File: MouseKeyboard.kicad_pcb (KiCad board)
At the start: 2 copper layers, 83.8 x 55.9 mm, 20 parts, among them IC1 ATMEGA328P-P, J1 USB, SW1 SW_PUSH, SW2 SW_PUSH, SW3 SW_PUSH, SW4 SW_PUSH, SW5 SW_PUSH, SW6 SW_PUSH, SW7 SW_PUSH, SW8 SPST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

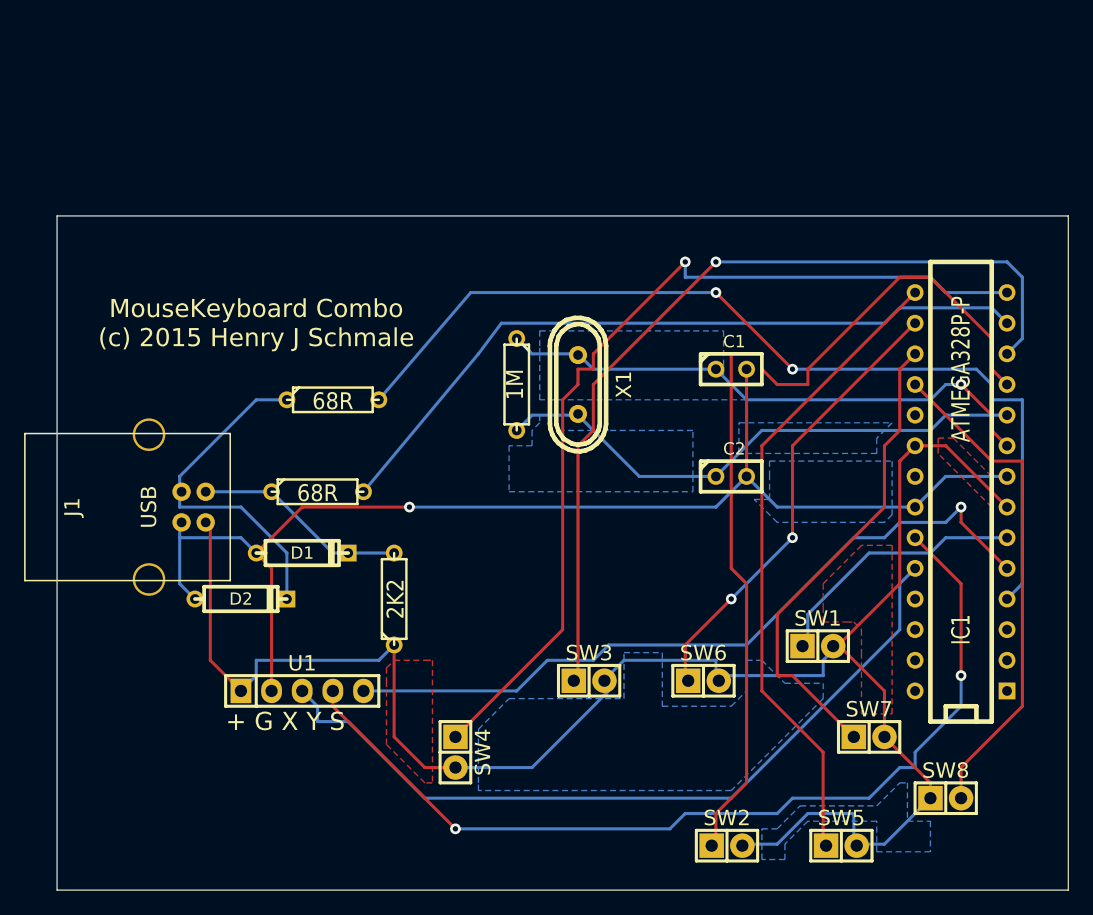
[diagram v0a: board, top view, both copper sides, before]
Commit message: Shrunk the PCB Design
* The PCB is roughly 20% Smaller than before
* \todo fix autorouting errors
* \todo perform DRC
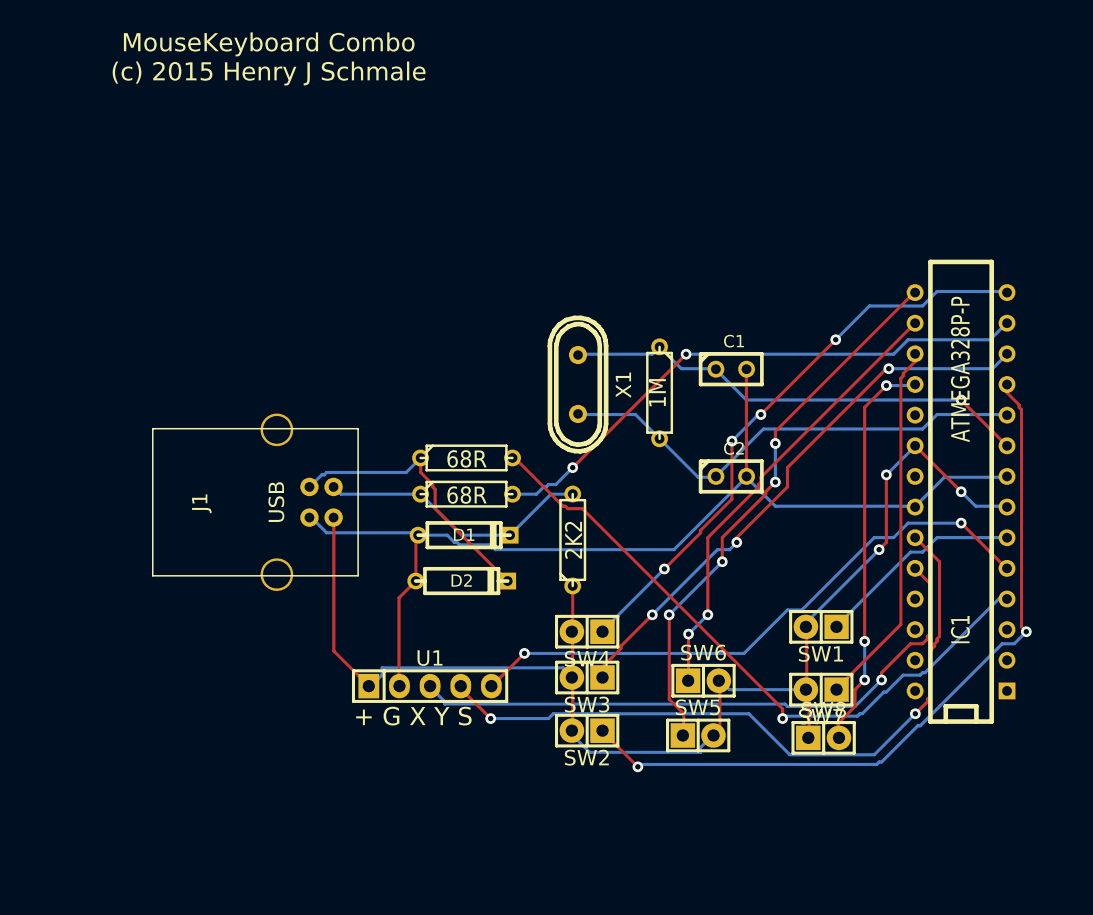
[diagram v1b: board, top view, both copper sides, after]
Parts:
- moved D2 18.4 mm to (132.6, 109.0)
- moved R1 15.6 mm to (141.8, 105.6)
- moved SW2 15.0 mm to (143.0, 121.4), turned to 180 degrees
- moved SW5 15.0 mm to (152.2, 121.8)
- moved SW4 14.8 mm to (143.0, 113.2), turned to 180 degrees
- moved D1 13.5 mm to (132.8, 105.2)
- moved R3 12.4 mm to (133.0, 101.8)
- moved R2 12.1 mm to (133.0, 98.8)
- moved R4 11.9 mm to (149.0, 93.4)
- moved SW8 11.3 mm to (162.6, 122.0)
- moved J1 10.6 mm to (117.3, 102.5)
- moved U1 10.6 mm to (130.0, 117.7)
- moved SW7 5.58 mm to (162.4, 118.0), turned to 180 degrees
- moved SW1 1.62 mm to (162.4, 112.8), turned to 180 degrees
- moved SW3 0.31 mm to (143.0, 117.0), turned to 180 degrees
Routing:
- net +5V: track 152.9 -> 110.4 mm, vias 0 -> 3
- net Net-(IC1-Pad14): track 76.5 -> 48.4 mm, vias 1 -> 4
- net Net-(IC1-Pad12): track 72.4 -> 46.6 mm, vias 1 -> 3
- net Net-(IC1-Pad4): track 78.9 -> 54.6 mm, vias 2 -> 1
- net Net-(IC1-Pad23): track 78.0 -> 58.2 mm
- net GND: track 101.9 -> 86.3 mm, vias 1 -> 0
- net Net-(IC1-Pad11): track 76.8 -> 62.3 mm, vias 0 -> 2
- net Net-(IC1-Pad24): track 65.3 -> 51.2 mm, vias 0 -> 1
- net Net-(IC1-Pad13): track 61.0 -> 46.9 mm, vias 0 -> 2
- net Net-(IC1-Pad5): track 62.5 -> 50.2 mm, vias 1 -> 2
- net Net-(IC1-Pad17): track 39.9 -> 30.6 mm
- net Net-(IC1-Pad18): track 41.6 -> 33.4 mm, vias 0 -> 3
- net Net-(IC1-Pad15): track 53.4 -> 45.9 mm, vias 0 -> 4
- net XTAL1: track 46.3 -> 39.5 mm
- net XTAL2: track 45.6 -> 40.0 mm
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- removed copper zone on B.Cu, net +5V
- removed copper zone on F.Cu, net +5V
- removed copper zone on B.Cu, net GND
- removed copper zone on B.Cu, net XTAL1
- removed copper zone on B.Cu, net XTAL2
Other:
- board outline removed

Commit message: Improved PCB Design
* Changed Text Size
* Moved Text Around
* DRC
* Improoved Routing

\todo Copper Infill
\todo Dimensioning
\todo Board Cut Lines
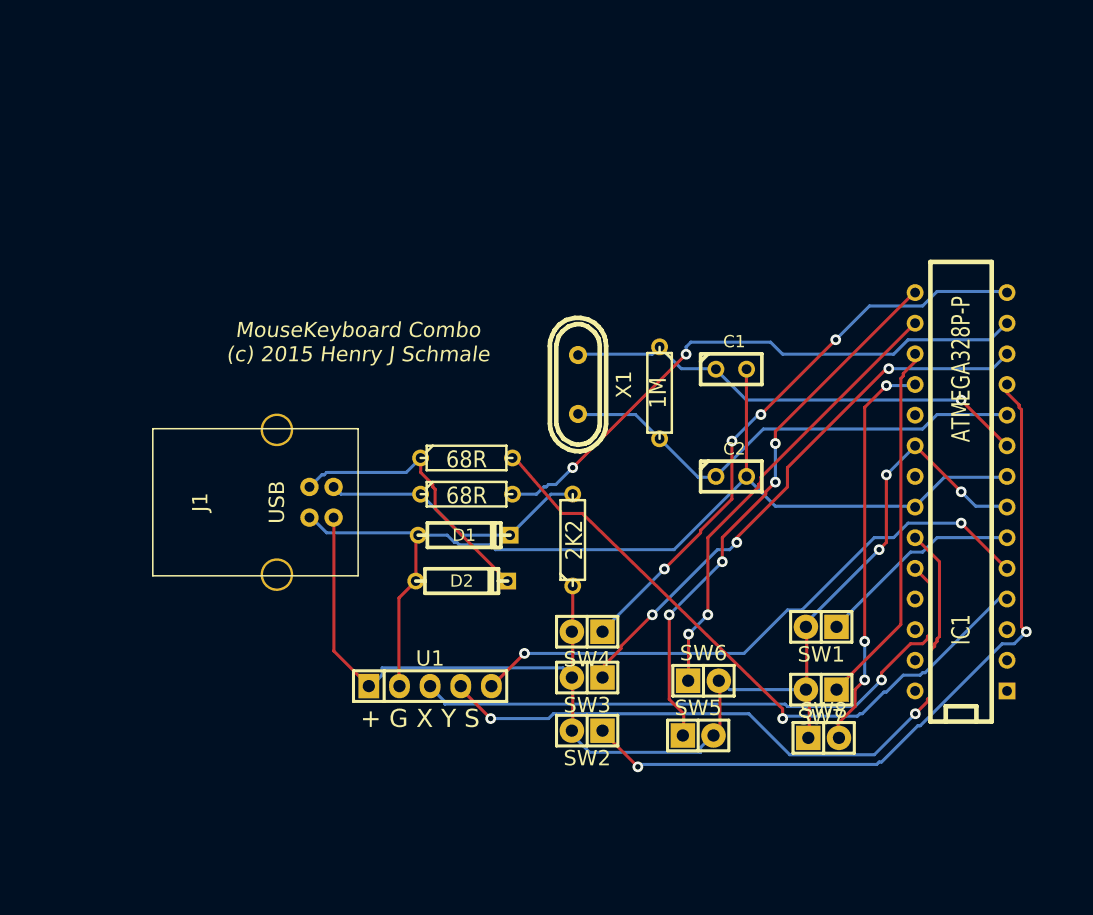
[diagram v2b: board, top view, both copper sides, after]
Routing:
- net Net-(IC1-Pad13): track 46.9 -> 48.1 mm
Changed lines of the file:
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@@
     (links 43)
     (no_connects 0)
-    (area 101.2 62.8 181.2 125)
+    (area 106.6 82 181 125.2)
     (thickness 1.6)
     (drawings 2)
-    (tracks 340)
+    (tracks 344)
     (zones 0)
     (modules 20)
@@
       (net 3 XTAL2))
   )
-  (gr_text "+ G X Y S\n" (at 123.63 120.25) (layer F.SilkS)
+  (gr_text "+ G X Y S\n" (at 124.2 120.4) (layer F.SilkS)
     (effects (font (size 1.5 1.5) (thickness 0.3)) (justify left))
   )
-  (gr_text "MouseKeyboard Combo\n(c) 2015 Henry J Schmale" (at 116.6 65.6) (layer F.SilkS)
-    (effects (font (size 1.5 1.5) (thickness 0.3)))
+  (gr_text "MouseKeyboard Combo\n(c) 2015 Henry J Schmale" (at 124 89.2) (layer F.SilkS)
+    (effects (font (size 1.25 1.25) (thickness 0.25) italic))
   )
   (segment (start 153.67 91.44) (end 153.6 91.4) (width 0.254) (layer B.Cu) (net 1) (status 80000))
@@
   (segment (start 120 101.2) (end 119.98002 101.2) (width 0.254) (layer B.Cu) (net 5) (status 80000))
   (segment (start 136.81 98.8) (end 137 98.8) (width 0.254) (layer F.Cu) (net 8) (status 80000))
-  (segment (start 137 98.8) (end 141 102.8) (width 0.254) (layer F.Cu) (net 8) (status 80000))
-  (segment (start 141 102.8) (end 141.2 102.8) (width 0.254) (layer F.Cu) (net 8) (status 80000))
-  (segment (start 141.2 102.8) (end 141.4 103) (width 0.254) (layer F.Cu) (net 8) (status 80000))
-  (segment (start 141.4 103) (end 142.6 103) (width 0.254) (layer F.Cu) (net 8) (status 80000))
-  (segment (start 142.6 103) (end 159.2 119.6) (width 0.254) (layer F.Cu) (net 8) (status 80000))
+  (segment (start 137 98.8) (end 140.8 103.2) (width 0.254) (layer F.Cu) (net 8) (status 80000))
+  (segment (start 140.8 103.2) (end 140.8 103.4) (width 0.254) (layer F.Cu) (net 8) (status 80000))
+  (segment (start 140.8 103.4) (end 141.2 103.4) (width 0.254) (layer F.Cu) (net 8) (status 80000))
+  (segment (start 141.2 103.4) (end 142.6 103.4) (width 0.254) (layer F.Cu) (net 8) (status 80000))
+  (segment (start 142.6 103.4) (end 159.2 119.6) (width 0.254) (layer F.Cu) (net 8) (status 80000))
   (segment (start 159.2 119.6) (end 159.2 120.4) (width 0.254) (layer F.Cu) (net 8) (status 80000))
   (via (at 159.2 120.4) (size 0.889) (layers F.Cu B.Cu) (net 8) (status 80000))
@@
   (segment (start 144.2 116.2) (end 144.2 117) (width 0.254) (layer F.Cu) (net 13) (status 80000))
   (segment (start 144.2 117) (end 144.27 117) (width 0.254) (layer F.Cu) (net 13) (status 80000))
+  (segment (start 151.2 90.2) (end 151.2 89.6) (width 0.254) (layer B.Cu) (net 14))
+  (segment (start 136.81 101.8) (end 138.8 101.8) (width 0.254) (layer B.Cu) (net 14) (status 80000))
+  (segment (start 139.4 101.2) (end 138.8 101.8) (width 0.254) (layer B.Cu) (net 14) (status 80000))
+  (segment (start 139.6 101.2) (end 139.4 101.2) (width 0.254) (layer B.Cu) (net 14) (status 80000))
+  (segment (start 139.8 101) (end 139.6 101.2) (width 0.254) (layer B.Cu) (net 14) (status 80000))
+  (segment (start 140.4 101) (end 139.8 101) (width 0.254) (layer B.Cu) (net 14) (status 80000))
+  (segment (start 141.8 99.6) (end 140.4 101) (width 0.254) (layer B.Cu) (net 14) (status 80000))
+  (via (at 141.8 99.6) (size 0.889) (layers F.Cu B.Cu) (net 14) (status 80000))
+  (segment (start 151.2 90.2) (end 141.8 99.6) (width 0.254) (layer F.Cu) (net 14) (status 80000))
+  (via (at 151.2 90.2) (size 0.889) (layers F.Cu B.Cu) (net 14) (status 80000))
+  (segment (start 168.4 90.2) (end 159.2 90.2) (width 0.254) (layer B.Cu) (net 14) (status 80000))
+  (segment (start 169.6 89) (end 168.4 90.2) (width 0.254) (layer B.Cu) (net 14) (status 80000))
+  (segment (start 176.4 89) (end 169.6 89) (width 0.254) (layer B.Cu) (net 14) (status 80000))
+  (segment (start 176.4 89) (end 177.8 87.6) (width 0.254) (layer B.Cu) (net 14) (status 80000))
+  (segment (start 158.2 89.2) (end 159.2 90.2) (width 0.254) (layer B.Cu) (net 14))
+  (segment (start 151.6 89.2) (end 158.2 89.2) (width 0.254) (layer B.Cu) (net 14))
+  (segment (start 151.2 89.6) (end 151.6 89.2) (width 0.254) (layer B.Cu) (net 14))
   (segment (start 177.8 87.63) (end 177.8 87.6) (width 0.254) (layer B.Cu) (net 14) (status 80000))
-  (segment (start 177.8 87.6) (end 176.4 89) (width 0.254) (layer B.Cu) (net 14) (status 80000))
-  (segment (start 176.4 89) (end 169.6 89) (width 0.254) (layer B.Cu) (net 14) (status 80000))
-  (segment (start 169.6 89) (end 168.4 90.2) (width 0.254) (layer B.Cu) (net 14) (status 80000))
-  (segment (start 168.4 90.2) (end 151.2 90.2) (width 0.254) (layer B.Cu) (net 14) (status 80000))
-  (via (at 151.2 90.2) (size 0.889) (layers F.Cu B.Cu) (net 14) (status 80000))
-  (segment (start 151.2 90.2) (end 141.8 99.6) (width 0.254) (layer F.Cu) (net 14) (status 80000))
-  (via (at 141.8 99.6) (size 0.889) (layers F.Cu B.Cu) (net 14) (status 80000))
-  (segment (start 141.8 99.6) (end 140.4 101) (width 0.254) (layer B.Cu) (net 14) (status 80000))
-  (segment (start 140.4 101) (end 139.8 101) (width 0.254) (layer B.Cu) (net 14) (status 80000))
-  (segment (start 139.8 101) (end 139.6 101.2) (width 0.254) (layer B.Cu) (net 14) (status 80000))
-  (segment (start 139.6 101.2) (end 139.4 101.2) (width 0.254) (layer B.Cu) (net 14) (status 80000))
-  (segment (start 139.4 101.2) (end 138.8 101.8) (width 0.254) (layer B.Cu) (net 14) (status 80000))
-  (segment (start 138.8 101.8) (end 136.81 101.8) (width 0.254) (layer B.Cu) (net 14) (status 80000))
   (segment (start 144.27 113.2) (end 144.2 113.2) (width 0.254) (layer B.Cu) (net 15) (status 80000))
   (segment (start 144.2 113.2) (end 149.4 108) (width 0.254) (layer B.Cu) (net 15) (status 80000))

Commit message: BoardDims
* Dim'd the board
* Board Cuts

\todo, fix silkscreening
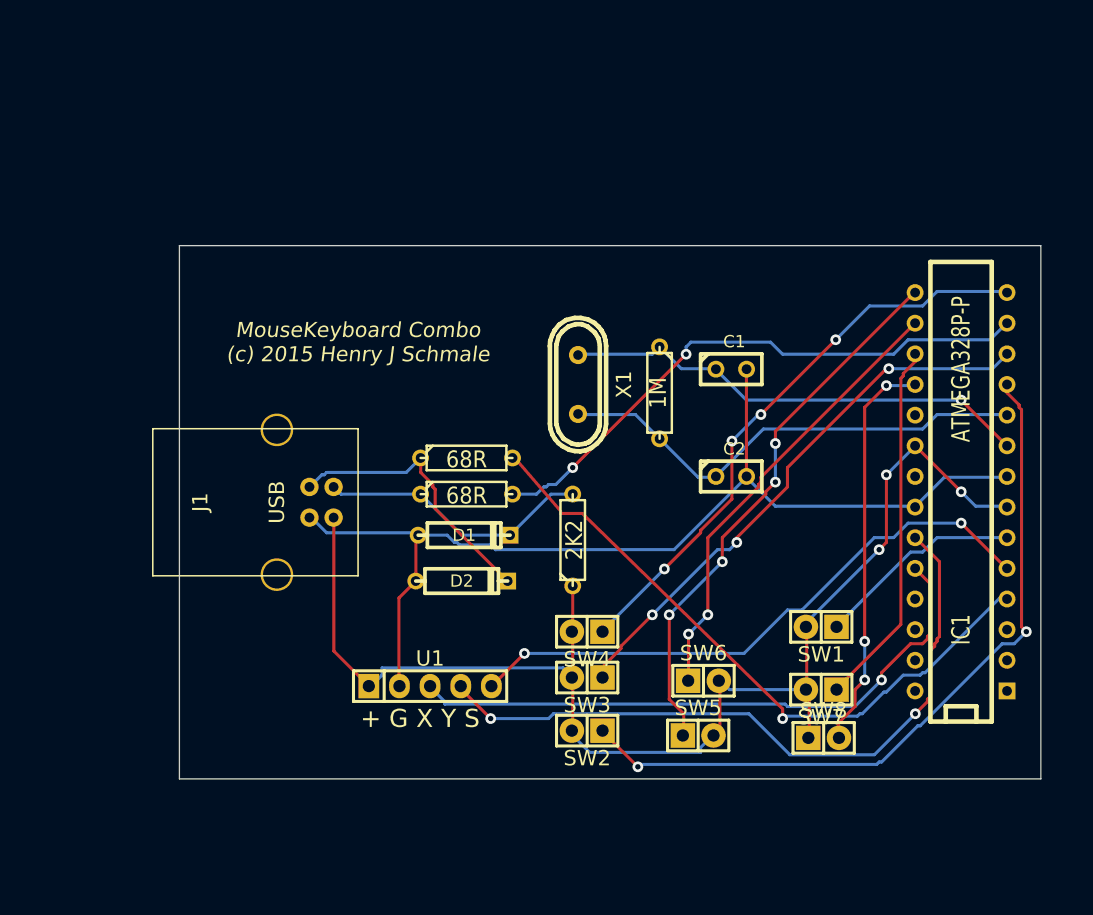
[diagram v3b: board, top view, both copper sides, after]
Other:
- board outline added: 71.4 x 44.2 mm
